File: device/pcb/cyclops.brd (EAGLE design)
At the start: 124.5 x 79.9 mm, 183 parts, among them Q1 SSM3K324, Q2 SSM3K324, Q3 SSM3K324, Q4 IRF510, U1 MCP4921, U10 ADG1201, U11 THS4281, U12 MAX4564, U13 ZXTD, U14 ZXTD, U15 OPA1664, U2 LT1931, U3 LT1764A, U31 TPS62153, U4 BD00FC0WEFJ, U5 TPS72325, U6 LT1711, U7 TLV3701, U8 ADR03, U9 LT1880

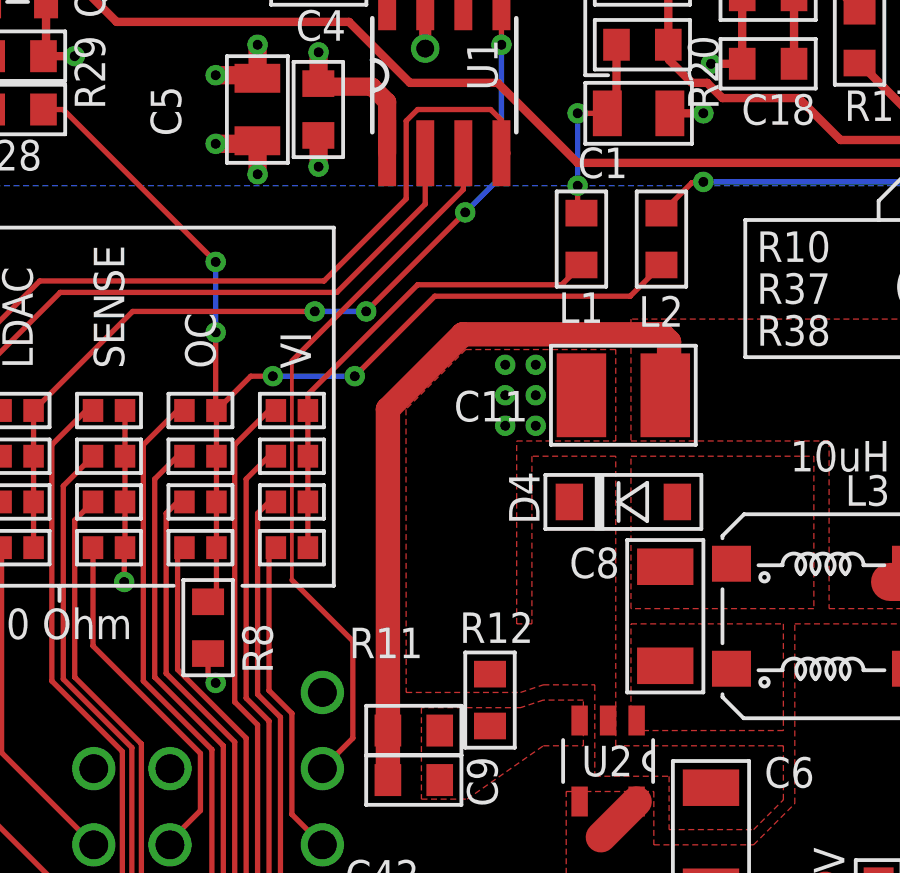
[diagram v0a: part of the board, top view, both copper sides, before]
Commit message: Fixed a couple circuit bugs found during prototype build.
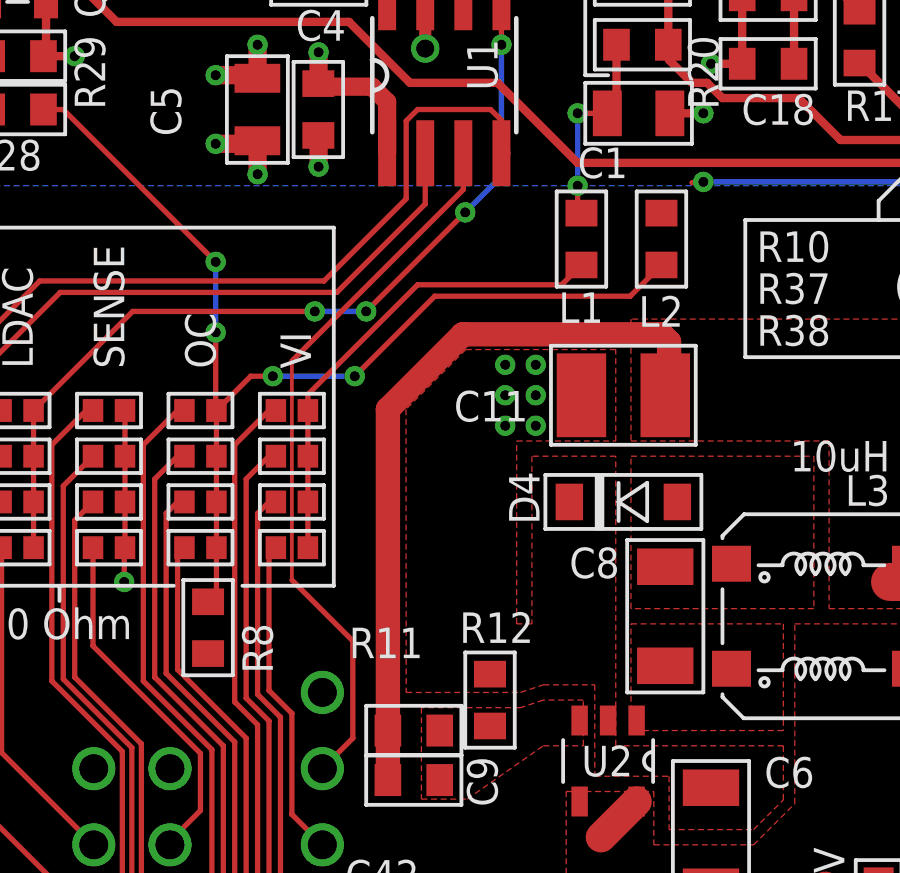
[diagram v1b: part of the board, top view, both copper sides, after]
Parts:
- D3: value MM3Z5V1 -> SZMM3Z5V1
- R1: value 110k -> 100k
- R8: value 110k -> 10k
- U10: value ADG1201 -> ADG1202
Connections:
- net OC0 renamed ~OC0
- net OC1 renamed ~OC1
- net OC2 renamed ~OC2
- net OC3 renamed ~OC3
- new net ~OVER_CURR: L2.1
- net +3V3: now also R8.2
- net -2.5V: no longer C15.2
- net GND: now also C15.2; no longer R8.2
- net OVER_CURR: no longer L2.1
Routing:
- net OVER_CURR: track 16.9 -> 15.4 mm
- net GND: track 107.2 -> 106.2 mm, vias 272 -> 271
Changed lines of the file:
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@@
 <layer number="23" name="tOrigins" color="15" fill="1" visible="yes" active="yes"/>
 <layer number="24" name="bOrigins" color="15" fill="1" visible="yes" active="yes"/>
-<layer number="25" name="tNames" color="7" fill="1" visible="yes" active="yes"/>
+<layer number="25" name="tNames" color="7" fill="1" visible="no" active="yes"/>
 <layer number="26" name="bNames" color="7" fill="1" visible="no" active="yes"/>
-<layer number="27" name="tValues" color="7" fill="1" visible="yes" active="yes"/>
+<layer number="27" name="tValues" color="7" fill="1" visible="no" active="yes"/>
 <layer number="28" name="bValues" color="7" fill="1" visible="no" active="yes"/>
-<layer number="29" name="tStop" color="7" fill="3" visible="yes" active="yes"/>
+<layer number="29" name="tStop" color="7" fill="3" visible="no" active="yes"/>
 <layer number="30" name="bStop" color="7" fill="6" visible="no" active="yes"/>
 <layer number="31" name="tCream" color="7" fill="4" visible="no" active="yes"/>
@@
 <attribute name="OC_FARNELL" value="1838919" x="55.499" y="55.76" size="1.778" layer="27" rot="R90" display="off"/>
 <attribute name="NAME" x="54.0696" y="57.531" size="1.016" layer="25" font="vector" ratio="18" rot="SR0"/>
-<attribute name="VALUE" x="57.411" y="54.229" size="1.016" layer="27" font="vector" ratio="18" rot="SR270"/>
+<attribute name="VALUE" x="56.5855" y="58.166" size="1.016" layer="27" font="vector" ratio="18" rot="SR270"/>
 </element>
 <element name="C22" library="cyclops" package="0805" value="1uF" x="60.833" y="52.19" smashed="yes">
@@
 <element name="J_VI1" library="jonnew" package="0402" value="0" x="20.574" y="42.418" smashed="yes"/>
 <element name="J_VI0" library="jonnew" package="0402" value="0" x="20.574" y="43.942" smashed="yes"/>
-<element name="R1" library="cyclops" package="0603" value="110k" x="32.258" y="56.134" smashed="yes" rot="R180">
+<element name="R1" library="cyclops" package="0603" value="100k" x="32.258" y="56.134" smashed="yes" rot="R180">
 <attribute name="MN" value="Panasonic" x="32.258" y="56.134" size="1.778" layer="27" rot="R180" display="off"/>
 <attribute name="DK" value="PxxxxHTR-ND" x="32.258" y="56.134" size="1.778" layer="27" rot="R180" display="off"/>
@@
 <attribute name="MPN" value="ERJ-3EKFxxxxV" x="44.069" y="59.309" size="1.778" layer="27" display="off"/>
 </element>
-<element name="D3" library="cyclops" package="SOD-323" value="MM3Z5V1" x="44.196" y="61.722" smashed="yes">
+<element name="D3" library="cyclops" package="SOD-323" value="SZMM3Z5V1" x="44.196" y="61.722" smashed="yes">
 <attribute name="NAME" x="43.688" y="62.992" size="1.016" layer="25" font="vector" ratio="18" rot="R90"/>
 <attribute name="VALUE" x="44.831" y="62.992" size="1.016" layer="27" font="vector" ratio="18" rot="R90"/>
@@
 <attribute name="VALUE" x="46.609" y="51.181" size="1.016" layer="27" font="vector" ratio="18" align="center-left"/>
 </element>
-<element name="R8" library="cyclops" package="0603" value="110k" x="17.78" y="36.703" smashed="yes" rot="R270">
+<element name="R8" library="cyclops" package="0603" value="10k" x="17.78" y="36.703" smashed="yes" rot="R270">
 <attribute name="MN" value="Panasonic" x="17.78" y="36.703" size="1.016" layer="27" font="vector" rot="R270" display="off"/>
 <attribute name="DK" value="PxxxxHTR-ND" x="17.78" y="36.703" size="1.016" layer="27" font="vector" rot="R270" display="off"/>
@@
 <attribute name="VALUE" x="56.709" y="47.169" size="1.016" layer="27" font="vector" ratio="18" rot="SR0"/>
 </element>
-<element name="U10" library="jonnew" package="SOT23-6" value="ADG1201" x="48.133" y="56.515" smashed="yes" rot="R90">
+<element name="U10" library="jonnew" package="SOT23-6" value="ADG1202" x="48.133" y="56.515" smashed="yes" rot="R90">
 <attribute name="VALUE" x="45.085" y="53.594" size="1.016" layer="27" font="vector" ratio="18" rot="R270"/>
 <attribute name="NAME" x="43.688" y="53.467" size="1.016" layer="25" font="vector" ratio="18" rot="R270"/>
@@
 <wire x1="26.2636" y1="17.78" x2="26.2636" y2="15.494" width="0.254" layer="1"/>
 <wire x1="25.527" y1="18.796" x2="24.384" y2="18.796" width="0.254" layer="1"/>
+<contactref element="R8" pad="2"/>
+<wire x1="17.653" y1="20.447" x2="17.78" y2="35.8394" width="0" layer="19" extent="1-16"/>
 <wire x1="21.59" y1="6.604" x2="26.2636" y2="15.494" width="0" layer="19" extent="1-1"/>
 </signal>
@@
 <via x="46.355" y="53.848" extent="1-16" drill="0.3302"/>
 <wire x1="43.0784" y1="61.722" x2="42.037" y2="61.722" width="0.3048" layer="1"/>
-<contactref element="R8" pad="2"/>
-<via x="18.034" y="34.8615" extent="1-16" drill="0.3302"/>
 <contactref element="IND" pad="C1"/>
 <contactref element="C12" pad="2"/>
@@
 <via x="74.676" y="56.134" extent="1-16" drill="0.3302"/>
 <via x="75.438" y="56.134" extent="1-16" drill="0.3302"/>
-<wire x1="18.034" y1="34.8615" x2="17.78" y2="35.1155" width="0.1778" layer="1"/>
-<wire x1="17.78" y1="35.1155" x2="17.78" y2="35.8394" width="0.1778" layer="1"/>
 <wire x1="58.928" y1="43.3705" x2="57.9755" y2="44.323" width="0.4064" layer="1"/>
 <wire x1="57.9755" y1="44.323" x2="57.912" y2="44.323" width="0.4064" layer="1"/>
+<contactref element="C15" pad="2"/>
+<wire x1="53.721" y1="30.988" x2="52.2986" y2="27.686" width="0" layer="19" extent="1-1"/>
 </signal>
 <signal name="N$1">
@@
 </signal>
 <signal name="OVER_CURR">
-<contactref element="L2" pad="1"/>
 <contactref element="U10" pad="6"/>
 <via x="34.29" y="51.562" extent="1-16" drill="0.3302"/>
@@
 <wire x1="44.069" y1="51.562" x2="34.29" y2="51.562" width="0.1778" layer="16"/>
 <wire x1="34.29" y1="51.5366" x2="33.909" y2="51.5366" width="0.1778" layer="1"/>
-<wire x1="33.909" y1="51.5366" x2="32.893" y2="50.5206" width="0.1778" layer="1"/>
 <wire x1="34.29" y1="51.5366" x2="34.29" y2="51.562" width="0.1778" layer="1"/>
 </signal>
@@
 <wire x1="13.843" y1="60.325" x2="13.843" y2="66.167" width="0.2794" layer="1"/>
 </signal>
-<signal name="OC3">
+<signal name="~OC3">
 <contactref element="J_OC3" pad="2"/>
 <contactref element="UC" pad="A11"/>
@@
 <wire x1="10.8966" y1="39.37" x2="10.8966" y2="32.5374" width="0.1778" layer="1"/>
 </signal>
-<signal name="OC1">
+<signal name="~OC1">
 <contactref element="J_OC1" pad="2"/>
 <contactref element="UC" pad="A12"/>
@@
 <contactref element="-2.5V" pad="1"/>
 <contactref element="U5" pad="5"/>
-<contactref element="C15" pad="2"/>
 <contactref element="C16" pad="2"/>
 <contactref element="U15" pad="11"/>
@@
 <wire x1="13.9446" y1="36.0934" x2="13.9446" y2="39.37" width="0.1778" layer="1"/>
 </signal>
-<signal name="OC2">
+<signal name="~OC2">
 <contactref element="J_OC2" pad="2"/>
 <contactref element="UC" pad="A10"/>
@@
 <wire x1="17.526" y1="13.208" x2="19.05" y2="11.684" width="0.1778" layer="1"/>
 </signal>
-<signal name="OC0">
+<signal name="~OC0">
 <contactref element="J_OC0" pad="2"/>
 <contactref element="UC" pad="A13"/>
@@
 <wire x1="8.382" y1="40.3606" x2="7.8486" y2="40.894" width="0.1778" layer="1"/>
 </signal>
+<signal name="~OVER_CURR">
+<contactref element="L2" pad="1"/>
+</signal>
 </signals>

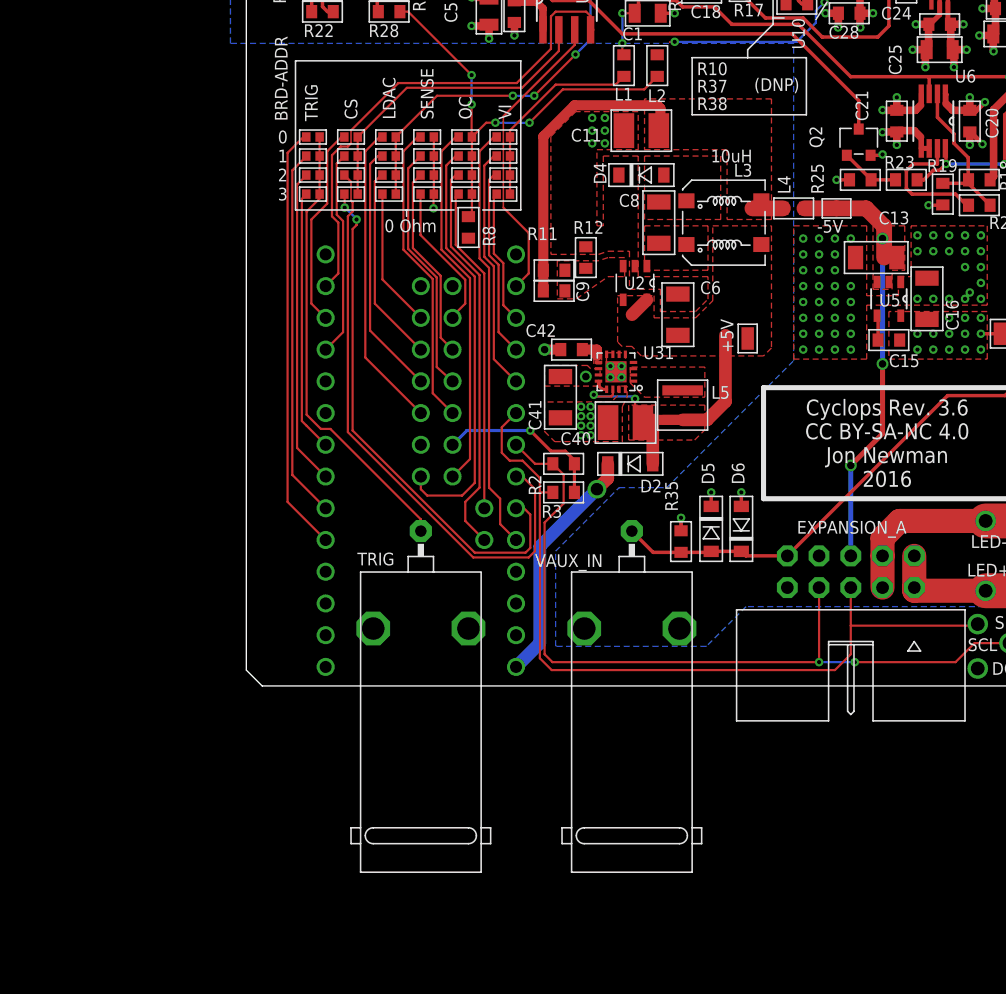
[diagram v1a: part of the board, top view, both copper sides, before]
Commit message: Minor circuit changes made during testing.
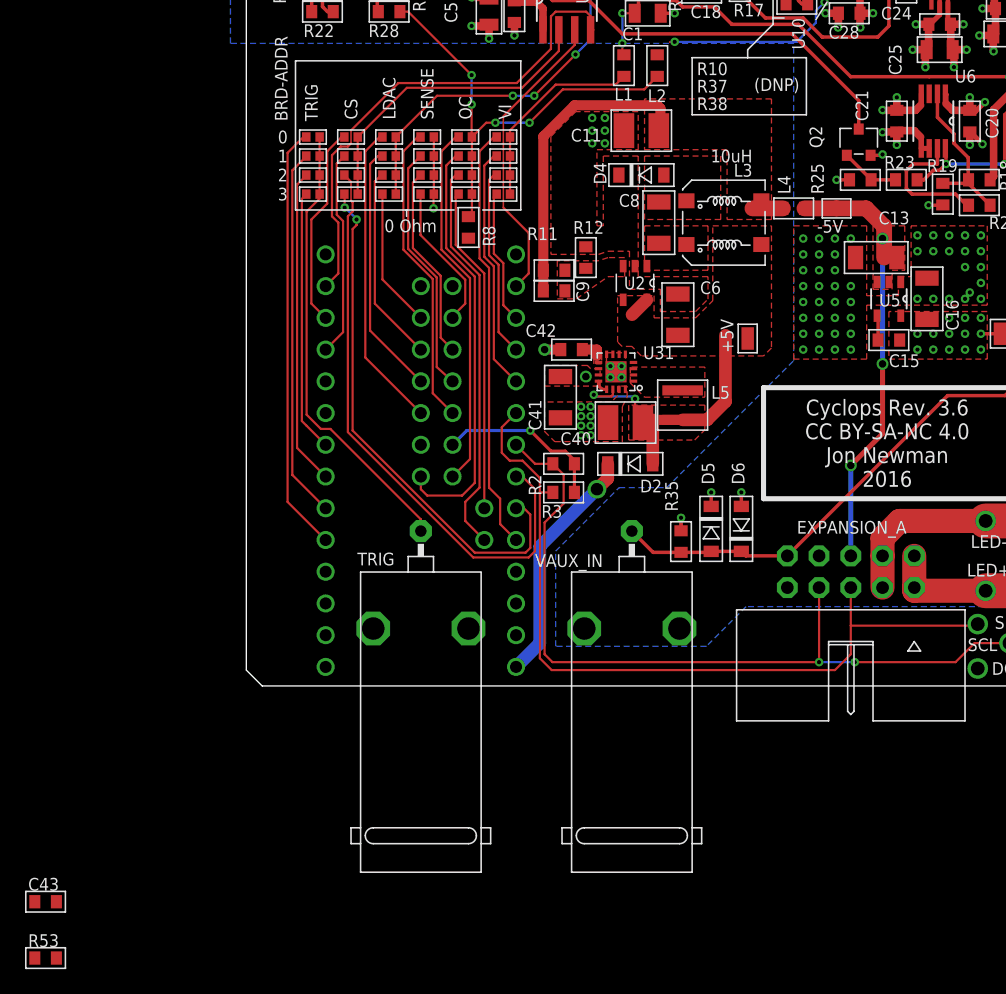
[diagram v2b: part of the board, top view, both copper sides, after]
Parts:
- added C43: (no value), cyclops:0603
- added R53: 0, cyclops:0603
- OC: value 569-0112-200 -> 569-0111-100
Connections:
- new net N$7: C43.1, R53.2, U6.3
- net GND: now also C43.2
- net VI_INTERNAL: now also R53.1; no longer U6.3
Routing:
- net VI_INTERNAL: track 44.6 -> 43.3 mm

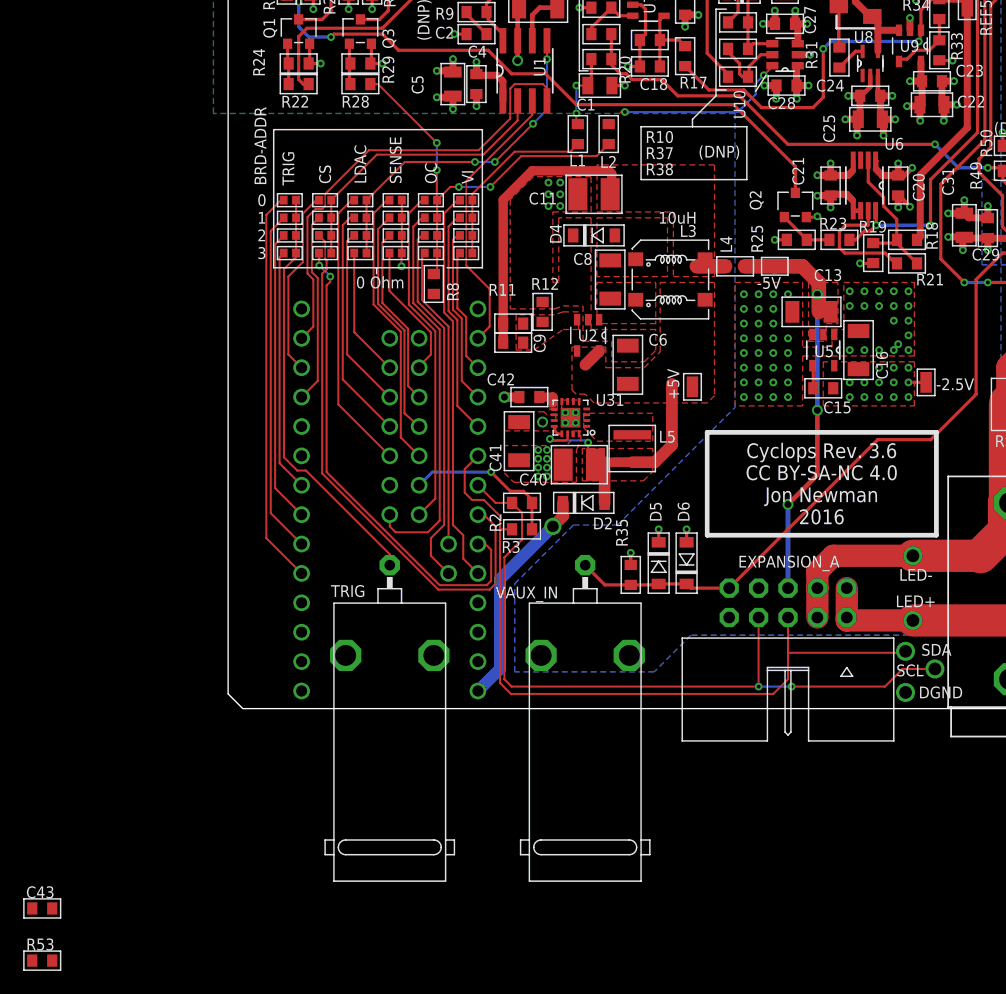
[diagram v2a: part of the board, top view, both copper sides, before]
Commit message: Changes from benchtop testing 3.6
- Buck got replaced with LT uModule to reduce switching noise
- low pass filter input to LED on circuit to prevent glitching.
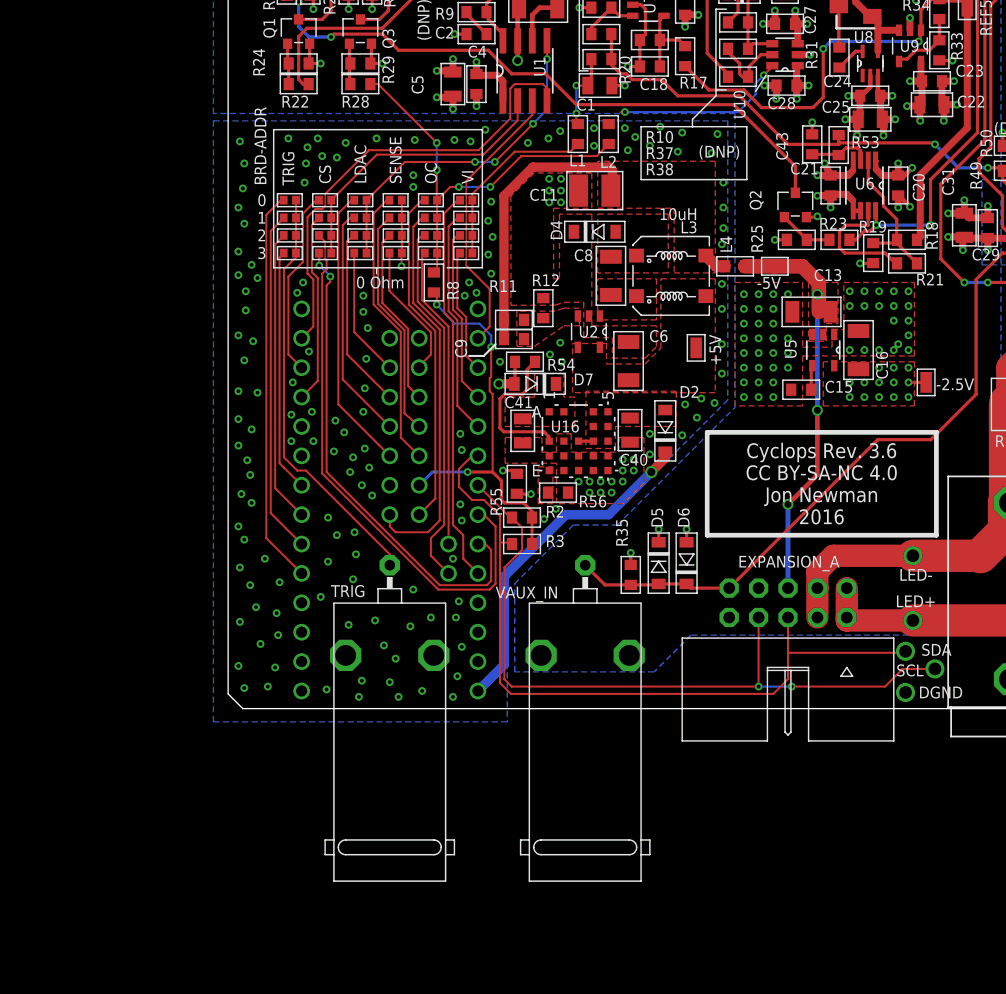
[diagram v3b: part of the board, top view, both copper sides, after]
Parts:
- removed C42: 3.3nF, jonnew:0603
- removed L5: XFL4020-222ME, jonnew:4020
- removed U31: TPS62153, jonnew:VQFN16
- added D7: 1N5819, jonnew:SOD123
- added R54: 100k, cyclops:0603
- added R55: 1M, cyclops:0603
- added R56: 165k, cyclops:0603
- added U16: (no value), jonnew:LGA21C127P5X5_625X625X242
- C40: value 22uF -> JMK212BJ106; device cyclops:1210 -> jonnew:0805
- C41: value 10uF -> TMK212AB7475KG-T; device jonnew:1206 -> jonnew:0805
- C43: value (none) -> 10nF
- R53: value 0 -> 100
- moved R53 98.5 mm to (52.8, 48.7), turned to 270 degrees
- moved C43 93.8 mm to (50.5, 48.8), turned to 90 degrees
- moved D2 9.40 mm to (37.8, 24.0), turned to 270 degrees
- moved C40 5.30 mm to (34.7, 24.1), turned to 270 degrees
- moved +5V 3.38 mm to (40.4, 31.2), turned to 180 degrees
- moved C15 1.91 mm to (49.5, 27.6), turned to 180 degrees
- moved R2 1.27 mm to (25.4, 16.5)
- moved R3 1.27 mm to (25.4, 14.2)
- moved C41 0.94 mm to (25.5, 24.0)
- moved D4 0.32 mm to (31.7, 41.2)
- moved R11 0.32 mm to (24.7, 33.6)
- moved R12 0.32 mm to (27.2, 34.6)
- moved C6 0.32 mm to (34.6, 30.0)
- moved C9 0.32 mm to (24.7, 31.9)
- moved L3 0.32 mm to (38.3, 37.4)
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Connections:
- removed net N$56: C42.1, U31.9
- removed net SW: L5.2, U31.1, U31.2, U31.3
- new net N$21: C41.1, D7.C, U16.A1, U16.A2
- new net N$23: R54.1, U16.C1
- new net N$38: R56.2, U16.E1
- net +15V: now also D7.A, R54.2, R55.1; no longer C41.1, U31.10, U31.11, U31.12, U31.13
- net +5V: now also U16.A4, U16.A5, U16.B4, U16.B5, U16.C3, U16.C4, U16.C5; no longer L5.1, U31.14
- net GND: now also R55.2, R56.1, U16.C2, U16.D1, U16.D2, U16.D3, U16.D4, U16.D5, U16.E2, U16.E3, U16.E4, U16.E5; no longer C42.2, U31.15, U31.16, U31.5, U31.6, U31.7, U31.8, U31.PAD
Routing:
- net +5V: track 24.6 -> 1.27 mm, vias 2 -> 0
- net +3V3: track 13.8 -> 34.4 mm, vias 1 -> 3
- net N$23: track 0.00 -> 12.8 mm
- net TEENSY_VIN: track 19.3 -> 29.5 mm
- net N$7: track 0.00 -> 5.41 mm
- net N$56: track 1.68 -> 0.00 mm
- net GND: track 106.2 -> 107.1 mm, vias 271 -> 419
- net SDA: track 64.4 -> 65.2 mm
- net VI_INTERNAL: track 43.3 -> 44.1 mm
- net SCL: track 63.9 -> 63.1 mm
- net +15V: track 52.8 -> 52.5 mm, vias 3 -> 4
- added copper zone on layer 1, net N$21
- added copper zone on layer 1, net N$38
- removed copper zone on layer 1, net N$56
- removed copper zone on layer 1, net SW

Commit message: Minor.
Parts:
- U10: value ADG1202 -> ADG1201
- U16: value (none) -> LTM8020
